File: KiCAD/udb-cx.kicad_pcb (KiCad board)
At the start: 4 copper layers, 18 x 16.5 mm, 15 parts, among them J1 SM04B-SRSS-TB(LF)(SN), J2 USB_C_Receptacle, U1 TPD4E05U06DQAR

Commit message: .
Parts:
- renumbered TP1 to TP-Gnd1, TP to TP-Vcc1
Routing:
- net D-: track 11.7 -> 12.9 mm
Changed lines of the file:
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@@
 		(descr "SMD rectangular pad as test Point, square 1.5mm side length")
 		(tags "test point SMD pad rectangle square")
-		(property "Reference" "TP1"
+		(property "Reference" "TP-Gnd1"
 			(at 0 1.648 0)
 			(layer "B.SilkS")
@@
 		(descr "SMD rectangular pad as test Point, square 1.5mm side length")
 		(tags "test point SMD pad rectangle square")
-		(property "Reference" "TP"
+		(property "Reference" "TP-Vcc1"
 			(at 0 1.648 0)
 			(layer "B.SilkS")
@@
 	)
 	(segment
+		(start 101.25 44.840721)
+		(end 101.590721 44.5)
+		(width 0.25)
+		(layer "F.Cu")
+		(net 3)
+	)
+	(segment
+		(start 101.25 45.695)
+		(end 101.25 44.840721)
+		(width 0.25)
+		(layer "F.Cu")
+		(net 3)
+	)
+	(segment
 		(start 107.346101 49.247793)
 		(end 107.351528 49.25322)
@@
 	)
 	(segment
-		(start 101.418 44.5)
-		(end 102 44.5)
-		(width 0.25)
-		(layer "F.Cu")
-		(net 3)
-	)
-	(segment
-		(start 101.25 45.695)
-		(end 101.25 44.668)
-		(width 0.25)
-		(layer "F.Cu")
-		(net 3)
-	)
-	(segment
 		(start 106.43974 49.247793)
 		(end 107.346101 49.247793)
@@
 	)
 	(segment
-		(start 101.25 44.668)
-		(end 101.418 44.5)
+		(start 101.590721 44.5)
+		(end 102 44.5)
 		(width 0.25)
 		(layer "F.Cu")
@@
 		(end 102.5 49.9)
 		(width 0.25)
+		(layer "F.Cu")
+		(net 10)
+	)
+	(segment
+		(start 102.5 51.1)
+		(end 102.5 49.9)
+		(width 0.25)

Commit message: .
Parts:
- removed U1: TPD4E05U06DQAR, PCM_SparkFun-Semiconductor-Standard:UFDFN-10_2.5x1.0mm_P0.5mm
- added Z1: TPD4E05U06DQAR, PCM_SparkFun-Semiconductor-Standard:UFDFN-10_2.5x1.0mm_P0.5mm, F.Cu at (103.0, 47.7)
- moved TP-Gnd1 1.48 mm to (104.3, 53.2)
- moved TP-Vcc1 1.48 mm to (101.7, 53.2)
- moved R3 0.09 mm to (110.7, 44.6)
- moved C1 0.09 mm to (109.2, 44.6)
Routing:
- net VCC: track 12.5 -> 14.4 mm
- net GND: track 14.3 -> 13.1 mm, vias 10 -> 12
- net Earth: vias 0 -> 4

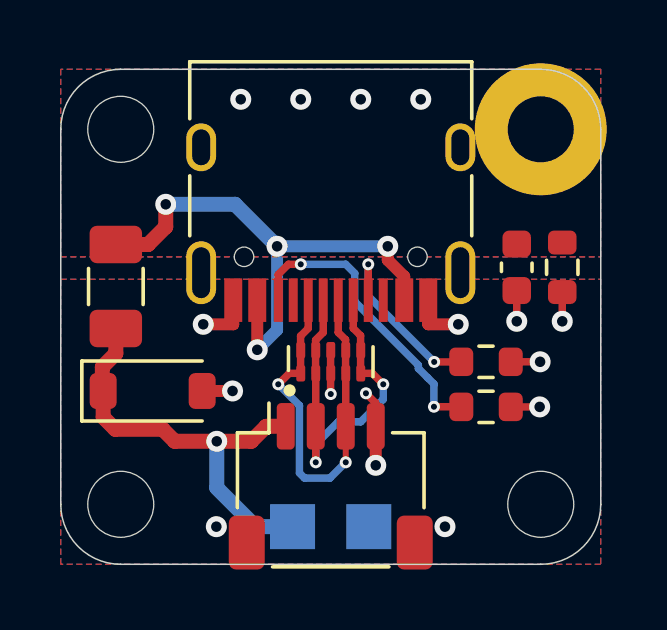
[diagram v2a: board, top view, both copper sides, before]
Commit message: mil sized traces
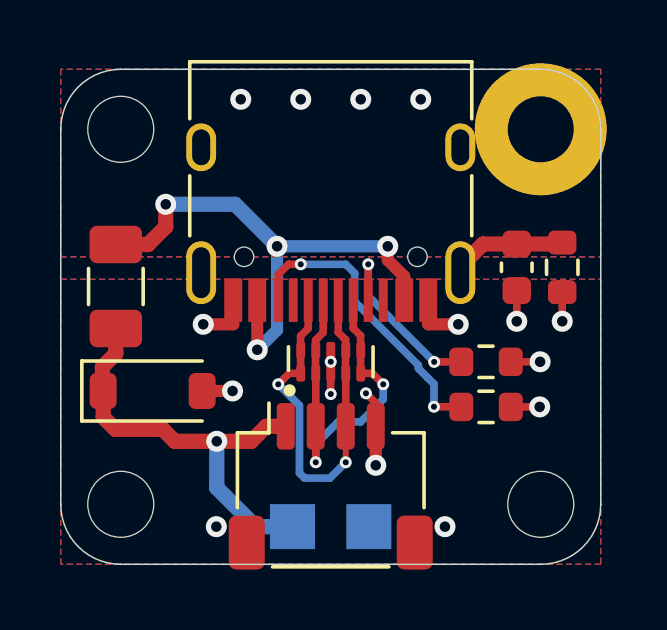
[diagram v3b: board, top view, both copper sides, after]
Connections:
- J1 pad MP: (no net) -> GND
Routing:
- net Earth: track 0.00 -> 3.93 mm
- net GND: vias 12 -> 13
